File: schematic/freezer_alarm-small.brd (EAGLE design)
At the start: 49.2 x 27.9 mm, 7 parts, among them IC1 DS18B20+, IC2 DS18B20+

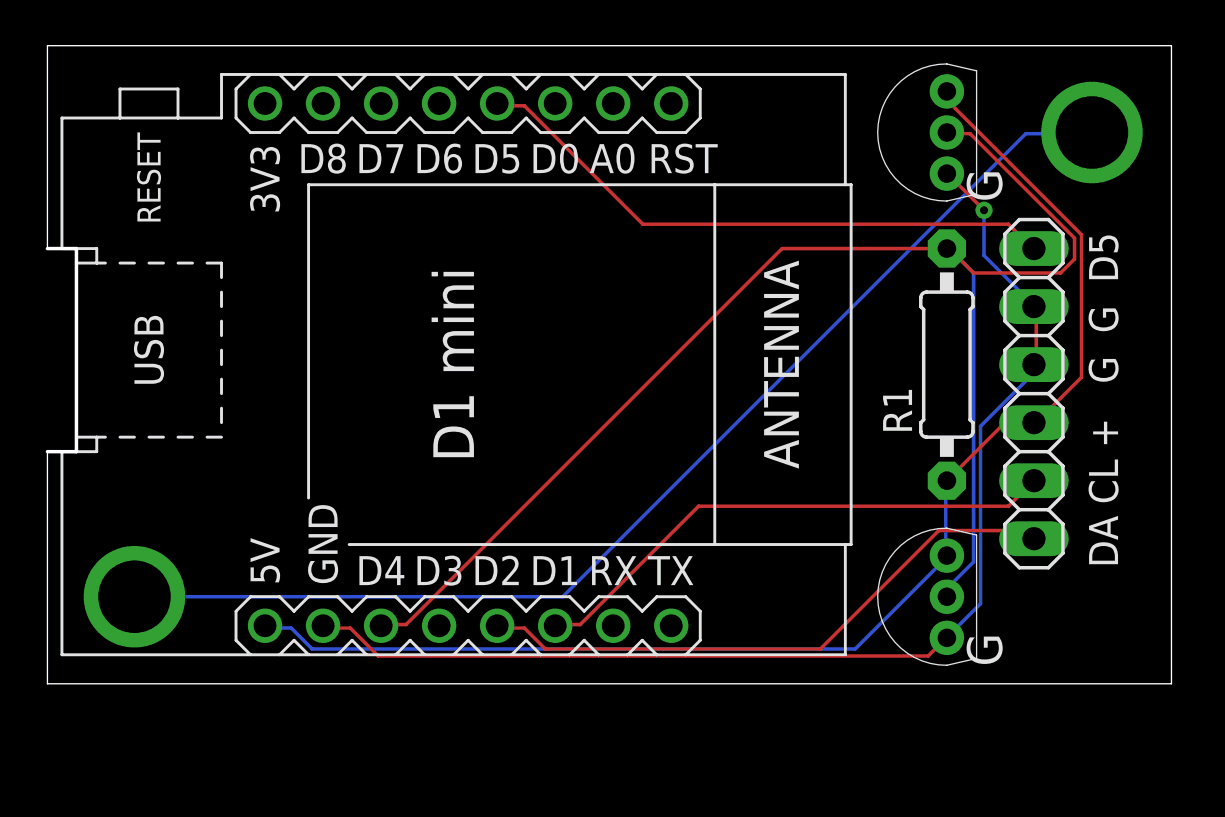
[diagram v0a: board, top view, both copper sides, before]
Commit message: Added notch for usb plug
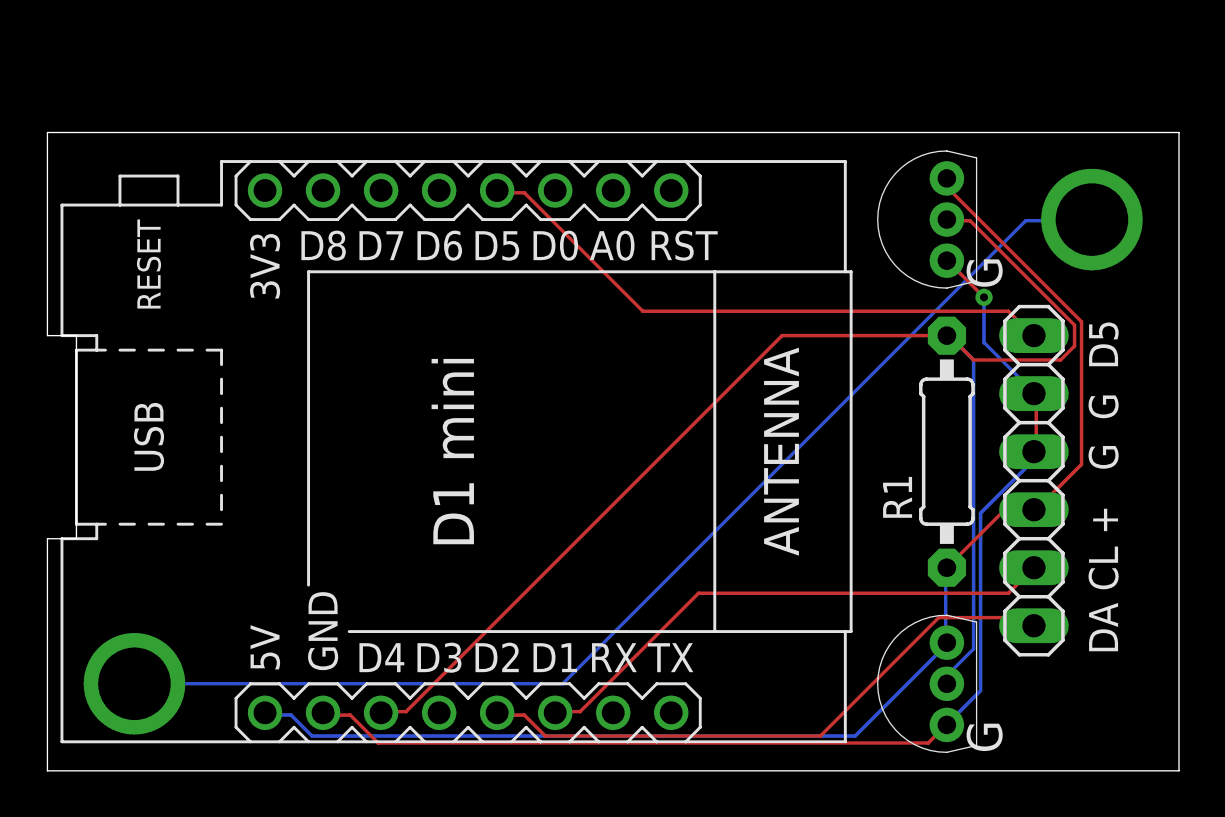
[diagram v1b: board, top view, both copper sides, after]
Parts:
- moved DISPLAY 3.81 mm to (43.2, 12.7)
- moved IC2 3.81 mm to (39.4, 24.1)
- moved MGT2 3.81 mm to (45.7, 24.1)
- moved R1 3.81 mm to (39.4, 14.0)
- moved W1 3.81 mm to (17.8, 14.0)
- moved IC1 3.81 mm to (39.4, 3.81)
- moved MGT1 3.81 mm to (3.81, 3.81)
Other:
- board size 49.2 x 27.9 mm -> 49.5 x 27.9 mm
